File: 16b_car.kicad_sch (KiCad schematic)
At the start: 34 parts, among them M1 Motor_DC, M2 Motor_DC, Q1 Q_NPN_BCE, Q2 Q_NPN_BCE, SW1 SW_DIP_x01, SW2 SW_DIP_x01, U2 LM317T, U3 LM317T

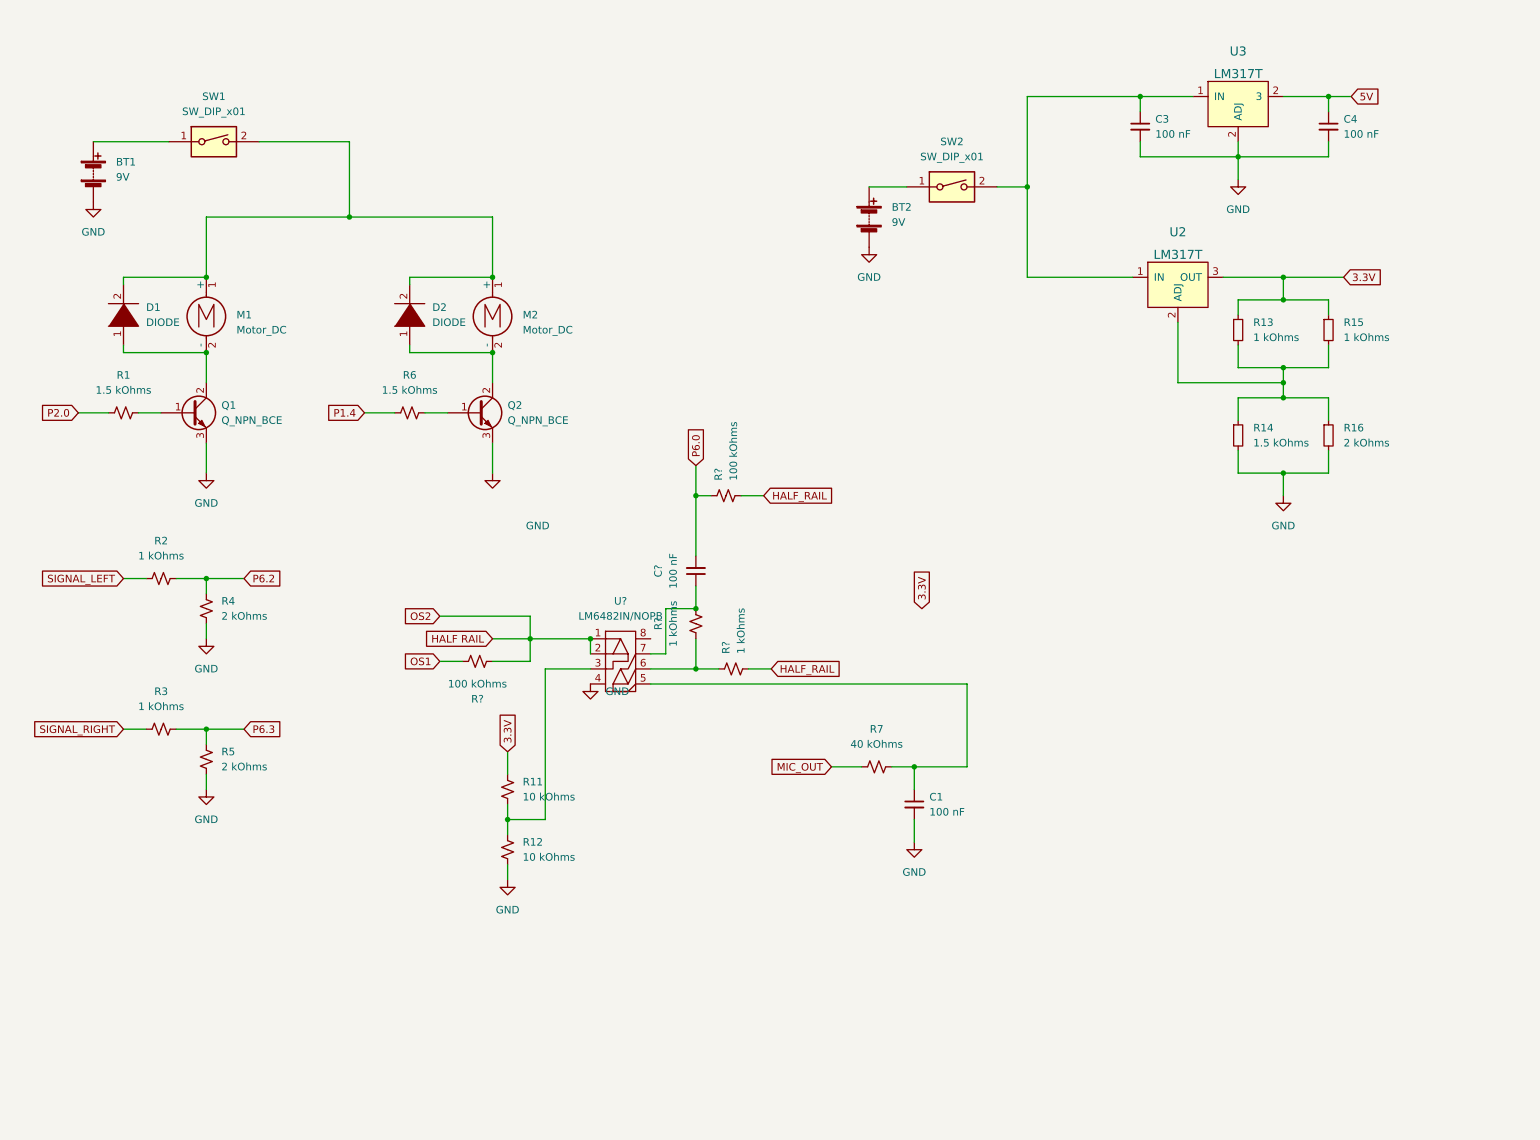
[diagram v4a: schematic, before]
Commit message: schematic done, some routing done
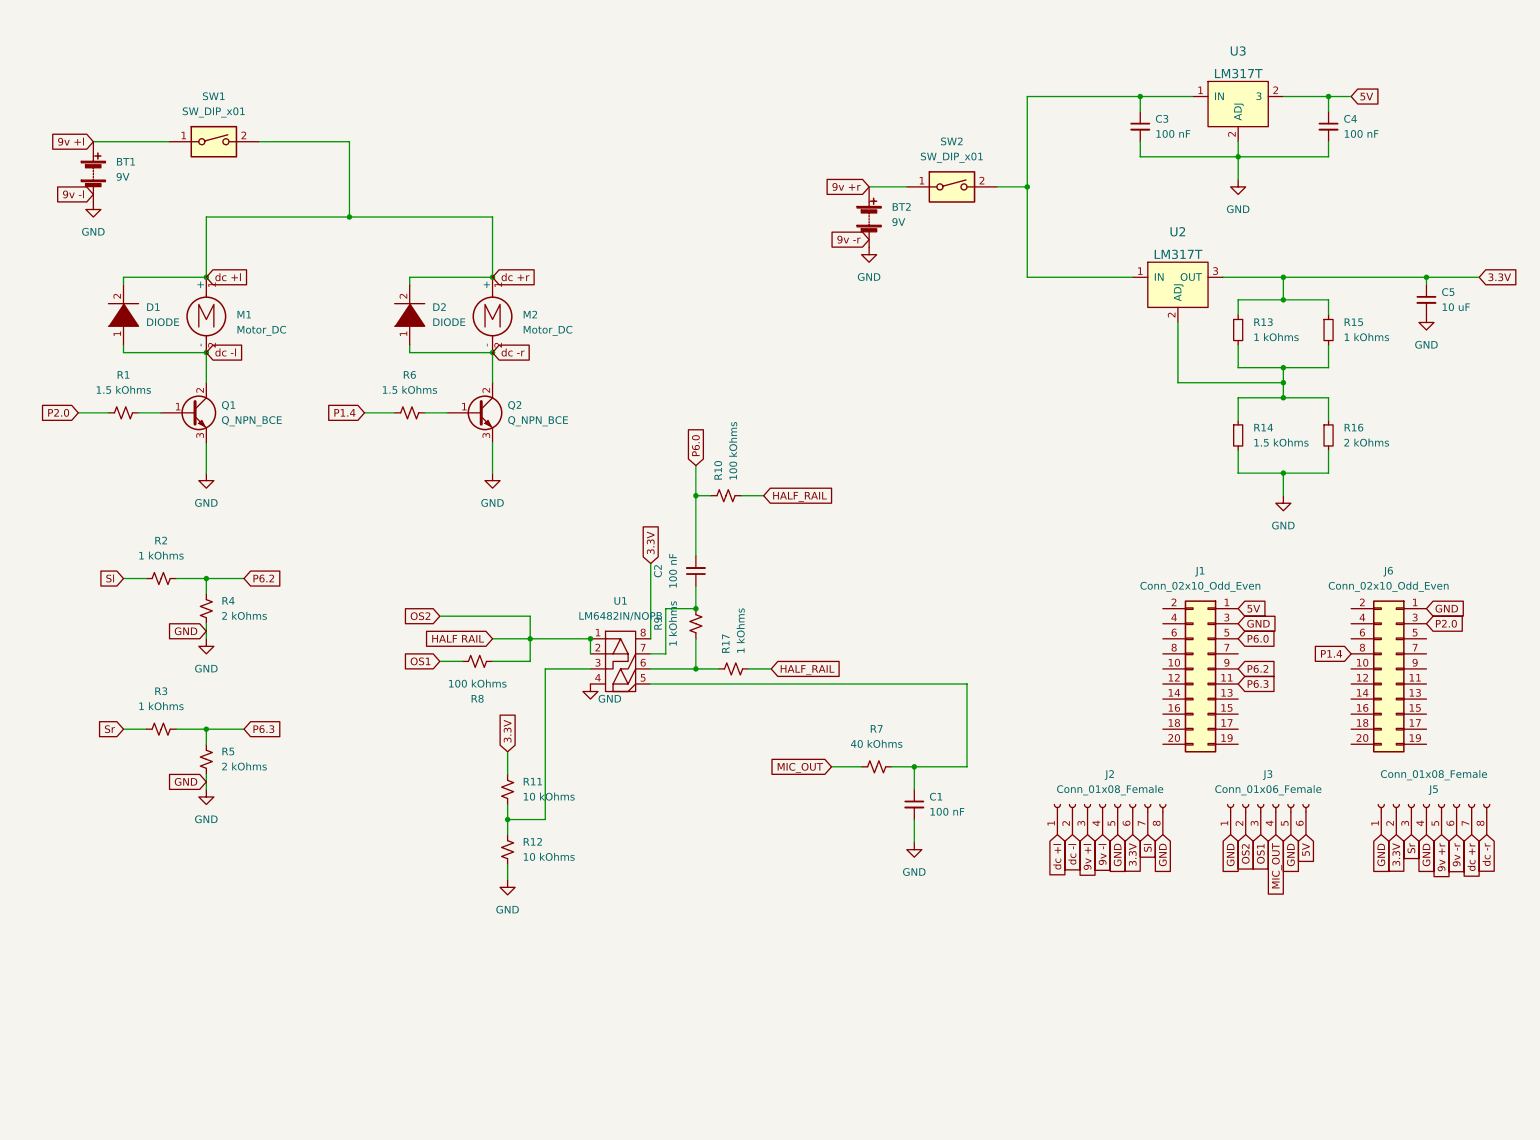
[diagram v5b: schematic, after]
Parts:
- added C5: 10 uF, Capacitor_SMD:C_0805_2012Metric_Pad1.18x1.45mm_HandSolder, symbol Device:C_Small
- added J1, J6: Conn_02x10_Odd_Even, Connector_PinSocket_2.54mm:PinSocket_2x10_P2.54mm_Vertical, symbol Connector_Generic:Conn_02x10_Odd_Even
- added J2, J5: Conn_01x08_Female, Connector_PinSocket_2.54mm:PinSocket_1x08_P2.54mm_Vertical, symbol Connector:Conn_01x08_Female
- added J3: Conn_01x06_Female, Connector_PinSocket_2.54mm:PinSocket_1x06_P2.54mm_Vertical, symbol Connector:Conn_01x06_Female
- C1: footprint (none) -> Capacitor_SMD:C_0805_2012Metric_Pad1.18x1.45mm_HandSolder
- C2: renamed from C?; footprint (none) -> Capacitor_SMD:C_0805_2012Metric_Pad1.18x1.45mm_HandSolder
- SW1: footprint sixteen_b_car:slide_switch -> sixteen_b_car:SW_DPDT_CK_JS202011JCQN
- gave numbers to parts that had none: 5
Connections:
- net 3.3V: now also U1.8, C5.1, J2.6 (Pin_6), J5.2 (Pin_2)
- net 5V: now also J1.1 (Pin_1), J3.6 (Pin_6)
- net GND: now also C5.2, J1.3 (Pin_3), J2.5 (Pin_5), J2.8 (Pin_8), J3.1 (Pin_1), J3.5 (Pin_5), J5.1 (Pin_1), J5.4 (Pin_4), J6.1 (Pin_1)
- net HALF RAIL: now also J3.2 (Pin_2)
- net MIC_OUT: now also J3.4 (Pin_4)
- net OS1: now also J3.3 (Pin_3)
- net P1.4: now also J6.8 (Pin_8)
- net P2.0: now also J6.3 (Pin_3)
- net P6.0: now also J1.5 (Pin_5)
- net P6.2: now also J1.9 (Pin_9)
- net P6.3: now also J1.11 (Pin_11)
- net dc -l: now reaches D1.1 (K), M1.2 (-), Q1.2 (C)
- net dc -l: now also J2.2 (Pin_2)
- net dc +l: now reaches D1.2 (A), D2.2 (A), M1.1 (+), M2.1 (+), SW1.2
- net dc +l: now also J2.1 (Pin_1), J5.7 (Pin_7)
- net 9v +l: now reaches BT1.1 (+), SW1.1
- net 9v +l: now also J2.3 (Pin_3)
- net 9v +r: now reaches BT2.1 (+), SW2.1
- net 9v +r: now also J5.5 (Pin_5)
- net dc -r: now reaches D2.1 (K), M2.2 (-), Q2.2 (C)
- net dc -r: now also J5.8 (Pin_8)
- net SIGNAL_LEFT renamed Sl
- net Sl: now also J2.7 (Pin_7)
- net SIGNAL_RIGHT renamed Sr
- net Sr: now also J5.3 (Pin_3)
- new net 9v -l: J2.4 (Pin_4)
- new net 9v -r: J5.6 (Pin_6)

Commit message: 0 errors, 0 warnings
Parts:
- added J4, J7, J8, J9: Conn_01x01_Female, Connector_PinSocket_2.54mm:PinSocket_1x01_P2.54mm_Vertical, symbol Connector:Conn_01x01_Female
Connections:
- net 9v -l is gone; now on net GND: J2.4 (Pin_4)
- net 9v -r is gone; now on net GND: J5.6 (Pin_6)
- net HALF RAIL is gone; now on net HALF_RAIL: J3.2 (Pin_2), R8.2, U1.1, U1.2
- net 3.3V: now also J8.1 (Pin_1)
- net 5V: now also J7.1 (Pin_1)
- net GND: now also J9.1 (Pin_1)
- net MIC_OUT: now also J4.1 (Pin_1)
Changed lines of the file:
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@@
     )
   )
-  (global_label "9v -l" (shape input) (at 208.28 147.32 270) (fields_autoplaced)
-    (effects (font (size 1.27 1.27)) (justify right))
-    (property "Intersheet References" "${INTERSHEET_REFS}" (id 0) (at 208.2006 155.1155 90)
+  (global_label "GND" (shape input) (at 208.28 147.32 270) (fields_autoplaced)
+    (effects (font (size 1.27 1.27)) (justify right))
+    (property "Intersheet References" "${INTERSHEET_REFS}" (id 0) (at 208.2006 153.6036 90)
       (effects (font (size 1.27 1.27)) (justify right) hide)
     )
@@
     )
   )
+  (global_label "MIC_OUT" (shape input) (at 26.67 184.15 270) (fields_autoplaced)
+    (effects (font (size 1.27 1.27)) (justify right))
+    (property "Intersheet References" "${INTERSHEET_REFS}" (id 0) (at 26.5906 194.4855 90)
+      (effects (font (size 1.27 1.27)) (justify right) hide)
+    )
+  )
   (global_label "GND" (shape input) (at 255.27 147.32 270) (fields_autoplaced)
     (effects (font (size 1.27 1.27)) (justify right))
@@
     )
   )
-  (global_label "9v -r" (shape input) (at 267.97 147.32 270) (fields_autoplaced)
-    (effects (font (size 1.27 1.27)) (justify right))
-    (property "Intersheet References" "${INTERSHEET_REFS}" (id 0) (at 267.8906 155.2364 90)
+  (global_label "GND" (shape input) (at 267.97 147.32 270) (fields_autoplaced)
+    (effects (font (size 1.27 1.27)) (justify right))
+    (property "Intersheet References" "${INTERSHEET_REFS}" (id 0) (at 267.8906 153.6036 90)
       (effects (font (size 1.27 1.27)) (justify right) hide)
     )
@@
     )
   )
+  (global_label "3.3V" (shape input) (at 80.01 184.15 270) (fields_autoplaced)
+    (effects (font (size 1.27 1.27)) (justify right))
+    (property "Intersheet References" "${INTERSHEET_REFS}" (id 0) (at 80.0894 190.6755 90)
+      (effects (font (size 1.27 1.27)) (justify right) hide)
+    )
+  )
   (global_label "Sl" (shape input) (at 43.18 104.14 180) (fields_autoplaced)
     (effects (font (size 1.27 1.27)) (justify right))
@@
     )
   )
-  (global_label "HALF RAIL" (shape input) (at 105.41 114.3 180) (fields_autoplaced)
-    (effects (font (size 1.27 1.27)) (justify right))
-    (property "Intersheet References" "${INTERSHEET_REFS}" (id 0) (at 93.5021 114.3794 0)
+  (global_label "HALF_RAIL" (shape input) (at 105.41 114.3 180) (fields_autoplaced)
+    (effects (font (size 1.27 1.27)) (justify right))
+    (property "Intersheet References" "${INTERSHEET_REFS}" (id 0) (at 93.5021 114.2206 0)
       (effects (font (size 1.27 1.27)) (justify right) hide)
     )
@@
     )
   )
+  (global_label "5V" (shape input) (at 53.34 184.15 270) (fields_autoplaced)
+    (effects (font (size 1.27 1.27)) (justify right))
+    (property "Intersheet References" "${INTERSHEET_REFS}" (id 0) (at 53.4194 188.8612 90)
+      (effects (font (size 1.27 1.27)) (justify right) hide)
+    )
+  )
   (global_label "OS2" (shape input) (at 96.52 110.49 180) (fields_autoplaced)
     (effects (font (size 1.27 1.27)) (justify right))
@@
     )
   )
-  (global_label "9v -l" (shape input) (at 38.1 39.37 180) (fields_autoplaced)
-    (effects (font (size 1.27 1.27)) (justify right))
-    (property "Intersheet References" "${INTERSHEET_REFS}" (id 0) (at 30.3045 39.2906 0)
+  (global_label "GND" (shape input) (at 38.1 39.37 180) (fields_autoplaced)
+    (effects (font (size 1.27 1.27)) (justify right))
+    (property "Intersheet References" "${INTERSHEET_REFS}" (id 0) (at 31.8164 39.2906 0)
       (effects (font (size 1.27 1.27)) (justify right) hide)
     )
@@
     )
   )
+  (global_label "GND" (shape input) (at 106.68 184.15 270) (fields_autoplaced)
+    (effects (font (size 1.27 1.27)) (justify right))
+    (property "Intersheet References" "${INTERSHEET_REFS}" (id 0) (at 106.6006 190.4336 90)
+      (effects (font (size 1.27 1.27)) (justify right) hide)
+    )
+  )
   (global_label "MIC_OUT" (shape input) (at 162.56 135.89 180) (fields_autoplaced)
     (effects (font (size 1.27 1.27)) (justify right))
@@
     )
   )
-  (global_label "9v -r" (shape input) (at 168.91 46.99 180) (fields_autoplaced)
-    (effects (font (size 1.27 1.27)) (justify right))
-    (property "Intersheet References" "${INTERSHEET_REFS}" (id 0) (at 160.9936 46.9106 0)
+  (global_label "GND" (shape input) (at 168.91 46.99 180) (fields_autoplaced)
+    (effects (font (size 1.27 1.27)) (justify right))
+    (property "Intersheet References" "${INTERSHEET_REFS}" (id 0) (at 162.6264 46.9106 0)
       (effects (font (size 1.27 1.27)) (justify right) hide)
     )
@@
     )
     (property "Datasheet" "" (id 3) (at 262.89 59.69 0)
+      (effects (font (size 1.27 1.27)) hide)
+    )
+    (pin "1")
+  )
+  (symbol (lib_id "Connector:Conn_01x01_Female") (at 26.67 179.07 90) (unit 1)
+    (in_bom yes) (on_board yes) (fields_autoplaced)
+    (property "Reference" "J4" (id 0) (at 27.94 178.4349 90)
+      (effects (font (size 1.27 1.27)) (justify right))
+    )
+    (property "Value" "Conn_01x01_Female" (id 1) (at 27.94 180.9749 90)
+      (effects (font (size 1.27 1.27)) (justify right))
+    )
+    (property "Footprint" "Connector_PinSocket_2.54mm:PinSocket_1x01_P2.54mm_Vertical" (id 2) (at 26.67 179.07 0)
+      (effects (font (size 1.27 1.27)) hide)
+    )
+    (property "Datasheet" "~" (id 3) (at 26.67 179.07 0)
       (effects (font (size 1.27 1.27)) hide)
     )
@@
     (pin "2")
   )
+  (symbol (lib_id "Connector:Conn_01x01_Female") (at 80.01 179.07 90) (unit 1)
+    (in_bom yes) (on_board yes) (fields_autoplaced)
+    (property "Reference" "J8" (id 0) (at 81.28 178.4349 90)
+      (effects (font (size 1.27 1.27)) (justify right))
+    )
+    (property "Value" "Conn_01x01_Female" (id 1) (at 81.28 180.9749 90)
+      (effects (font (size 1.27 1.27)) (justify right))
+    )
+    (property "Footprint" "Connector_PinSocket_2.54mm:PinSocket_1x01_P2.54mm_Vertical" (id 2) (at 80.01 179.07 0)
+      (effects (font (size 1.27 1.27)) hide)
+    )
+    (property "Datasheet" "~" (id 3) (at 80.01 179.07 0)
+      (effects (font (size 1.27 1.27)) hide)
+    )
+    (pin "1")
+  )
   (symbol (lib_id "Device:R_Small_US") (at 107.95 139.7 180) (unit 1)
     (in_bom yes) (on_board yes) (fields_autoplaced)
@@
     (pin "1")
     (pin "2")
+  )
+  (symbol (lib_id "Connector:Conn_01x01_Female") (at 53.34 179.07 90) (unit 1)
+    (in_bom yes) (on_board yes) (fields_autoplaced)
+    (property "Reference" "J7" (id 0) (at 54.61 178.4349 90)
+      (effects (font (size 1.27 1.27)) (justify right))
+    )
+    (property "Value" "Conn_01x01_Female" (id 1) (at 54.61 180.9749 90)
+      (effects (font (size 1.27 1.27)) (justify right))
+    )
+    (property "Footprint" "Connector_PinSocket_2.54mm:PinSocket_1x01_P2.54mm_Vertical" (id 2) (at 53.34 179.07 0)
+      (effects (font (size 1.27 1.27)) hide)
+    )
+    (property "Datasheet" "~" (id 3) (at 53.34 179.07 0)
+      (effects (font (size 1.27 1.27)) hide)
+    )
+    (pin "1")
   )
   (symbol (lib_id "Device:R_Small_US") (at 144.78 90.17 90) (unit 1)
@@
     (pin "9")
   )
+  (symbol (lib_id "Connector:Conn_01x01_Female") (at 106.68 179.07 90) (unit 1)
+    (in_bom yes) (on_board yes) (fields_autoplaced)
+    (property "Reference" "J9" (id 0) (at 107.95 178.4349 90)
+      (effects (font (size 1.27 1.27)) (justify right))
+    )
+    (property "Value" "Conn_01x01_Female" (id 1) (at 107.95 180.9749 90)
+      (effects (font (size 1.27 1.27)) (justify right))
+    )
+    (property "Footprint" "Connector_PinSocket_2.54mm:PinSocket_1x01_P2.54mm_Vertical" (id 2) (at 106.68 179.07 0)
+      (effects (font (size 1.27 1.27)) hide)
+    )
+    (property "Datasheet" "~" (id 3) (at 106.68 179.07 0)
+      (effects (font (size 1.27 1.27)) hide)
+    )
+    (pin "1")
+  )
   (symbol (lib_id "Device:R_Small_US") (at 139.7 111.76 0) (unit 1)
     (in_bom yes) (on_board yes) (fields_autoplaced)
@@
       (reference "J3") (unit 1) (value "Conn_01x06_Female") (footprint "Connector_PinSocket_2.54mm:PinSocket_1x06_P2.54mm_Vertical")
     )
+    (path "/37d3bf2b-1361-43a6-a660-8e584912f573"
+      (reference "J4") (unit 1) (value "Conn_01x01_Female") (footprint "Connector_PinSocket_2.54mm:PinSocket_1x01_P2.54mm_Vertical")
+    )
     (path "/c5bdada7-9304-4719-a5a3-b561328ed359"
       (reference "J5") (unit 1) (value "Conn_01x08_Female") (footprint "Connector_PinSocket_2.54mm:PinSocket_1x08_P2.54mm_Vertical")
@@
       (reference "J6") (unit 1) (value "Conn_02x10_Odd_Even") (footprint "Connector_PinSocket_2.54mm:PinSocket_2x10_P2.54mm_Vertical")
     )
+    (path "/6d2e8490-15e3-4782-90a8-05a3056780ed"
+      (reference "J7") (unit 1) (value "Conn_01x01_Female") (footprint "Connector_PinSocket_2.54mm:PinSocket_1x01_P2.54mm_Vertical")
+    )
+    (path "/416dfcbe-1eea-478d-8c11-0e6882ac1192"
+      (reference "J8") (unit 1) (value "Conn_01x01_Female") (footprint "Connector_PinSocket_2.54mm:PinSocket_1x01_P2.54mm_Vertical")
+    )
+    (path "/94ade9c6-2ad4-4cf9-9c37-4d26de34f693"
+      (reference "J9") (unit 1) (value "Conn_01x01_Female") (footprint "Connector_PinSocket_2.54mm:PinSocket_1x01_P2.54mm_Vertical")
+    )
     (path "/d977a94d-6c9a-43b3-ae85-8020f05b746b"
